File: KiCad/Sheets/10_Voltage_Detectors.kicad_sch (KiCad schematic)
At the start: 2 parts, among them U12 MVPDM-1PHS, U13 MVPDM-1PHS

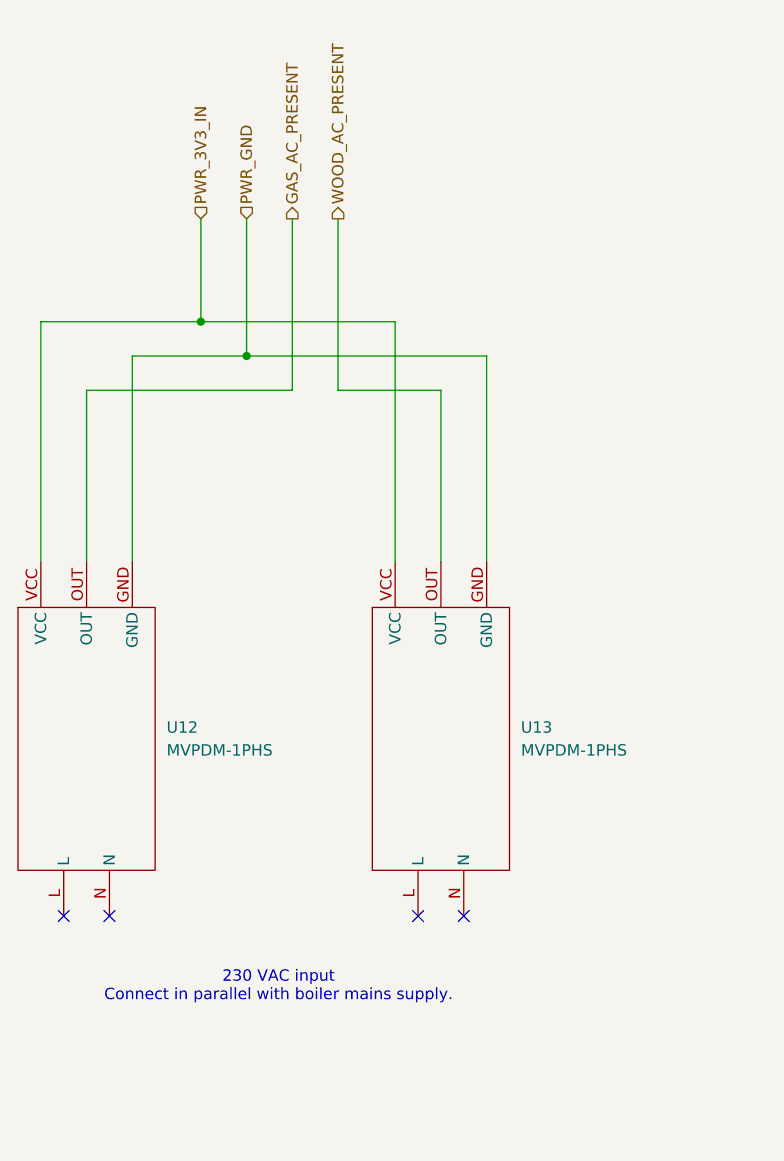
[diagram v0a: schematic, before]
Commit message: Footprints are created and assigned
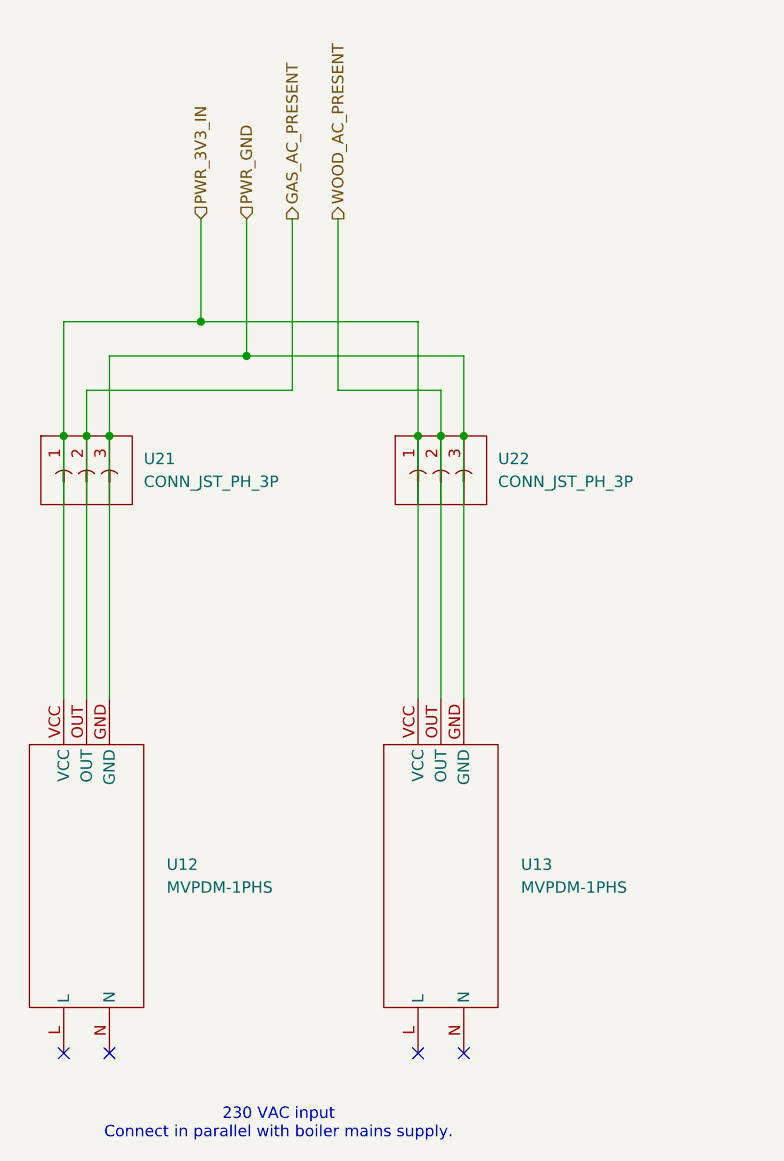
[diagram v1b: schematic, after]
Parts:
- added U21, U22: CONN_JST_PH_3P, Connector_JST:JST_PH_B3B-PH-K_1x03_P2.00mm_Vertical, symbol HMS_Symbols:CONN_JST_PH_3P
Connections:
- net GAS_AC_PRESENT: now also U21.2
- net PWR_3V3_IN: now also U21.1, U22.1
- net PWR_GND: now also U21.3, U22.3
- net WOOD_AC_PRESENT: now also U22.2
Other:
- moved on the sheet: U12, U13

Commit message: LEDs sheet added, schematic finished
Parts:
- U21: value CONN_JST_PH_3P -> GAS_AC_PRESENT_SOCKET
- U22: value CONN_JST_PH_3P -> WOOD_AC_PRESENT_SOCKET
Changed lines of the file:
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@@
 	)
 	(symbol
-		(lib_name "MVPDM-1PHS_1")
 		(lib_id "HMS_Symbols:MVPDM-1PHS")
 		(at 121.92 132.08 0)
@@
 			)
 		)
-		(property "Value" "CONN_JST_PH_3P"
+		(property "Value" "GAS_AC_PRESENT_SOCKET"
 			(at 128.27 91.4399 0)
 			(show_name no)
@@
 			)
 		)
-		(property "Value" "CONN_JST_PH_3P"
+		(property "Value" "WOOD_AC_PRESENT_SOCKET"
 			(at 167.64 91.4399 0)
 			(show_name no)

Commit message: Finished PCB
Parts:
- U21, U22: footprint Connector_JST:JST_PH_B3B-PH-K_1x03_P2.00mm_Vertical -> Connector_JST:JST_XH_B3B-XH-A_1x03_P2.50mm_Vertical
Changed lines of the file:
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@@
 			)
 		)
-		(property "Footprint" "Connector_JST:JST_PH_B3B-PH-K_1x03_P2.00mm_Vertical"
+		(property "Footprint" "Connector_JST:JST_XH_B3B-XH-A_1x03_P2.50mm_Vertical"
 			(at 121.92 97.282 0)
 			(hide yes)
@@
 			)
 		)
-		(property "Footprint" "Connector_JST:JST_PH_B3B-PH-K_1x03_P2.00mm_Vertical"
+		(property "Footprint" "Connector_JST:JST_XH_B3B-XH-A_1x03_P2.50mm_Vertical"
 			(at 161.29 97.282 0)
 			(hide yes)
